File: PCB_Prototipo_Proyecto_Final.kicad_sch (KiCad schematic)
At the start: 1 part

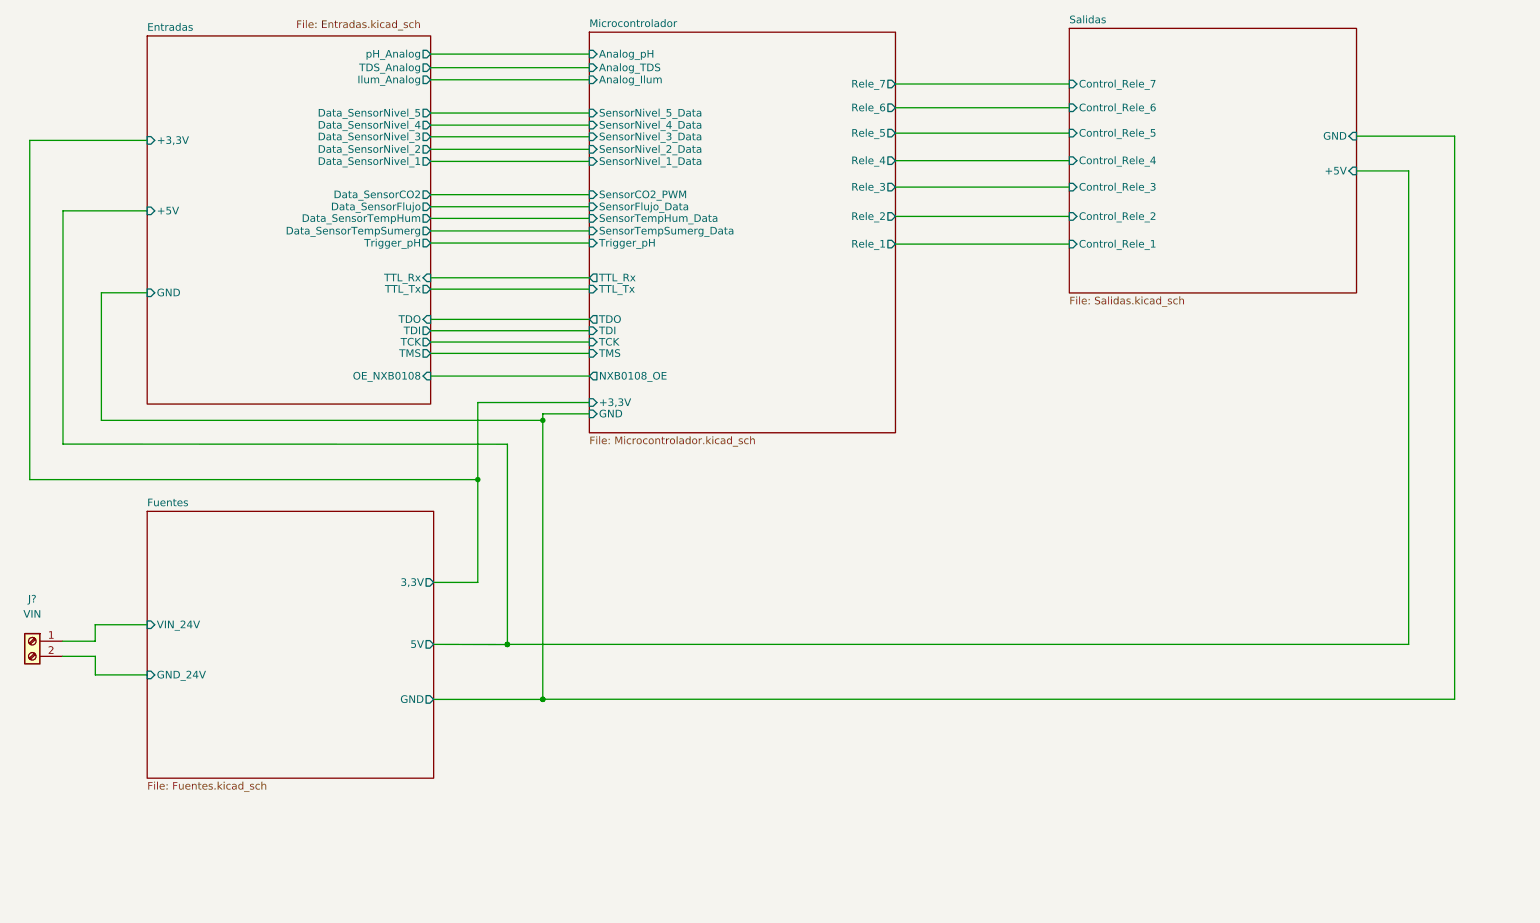
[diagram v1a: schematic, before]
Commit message: Modificación de posición de circ. filtrado y circ. de adaptación de tensión
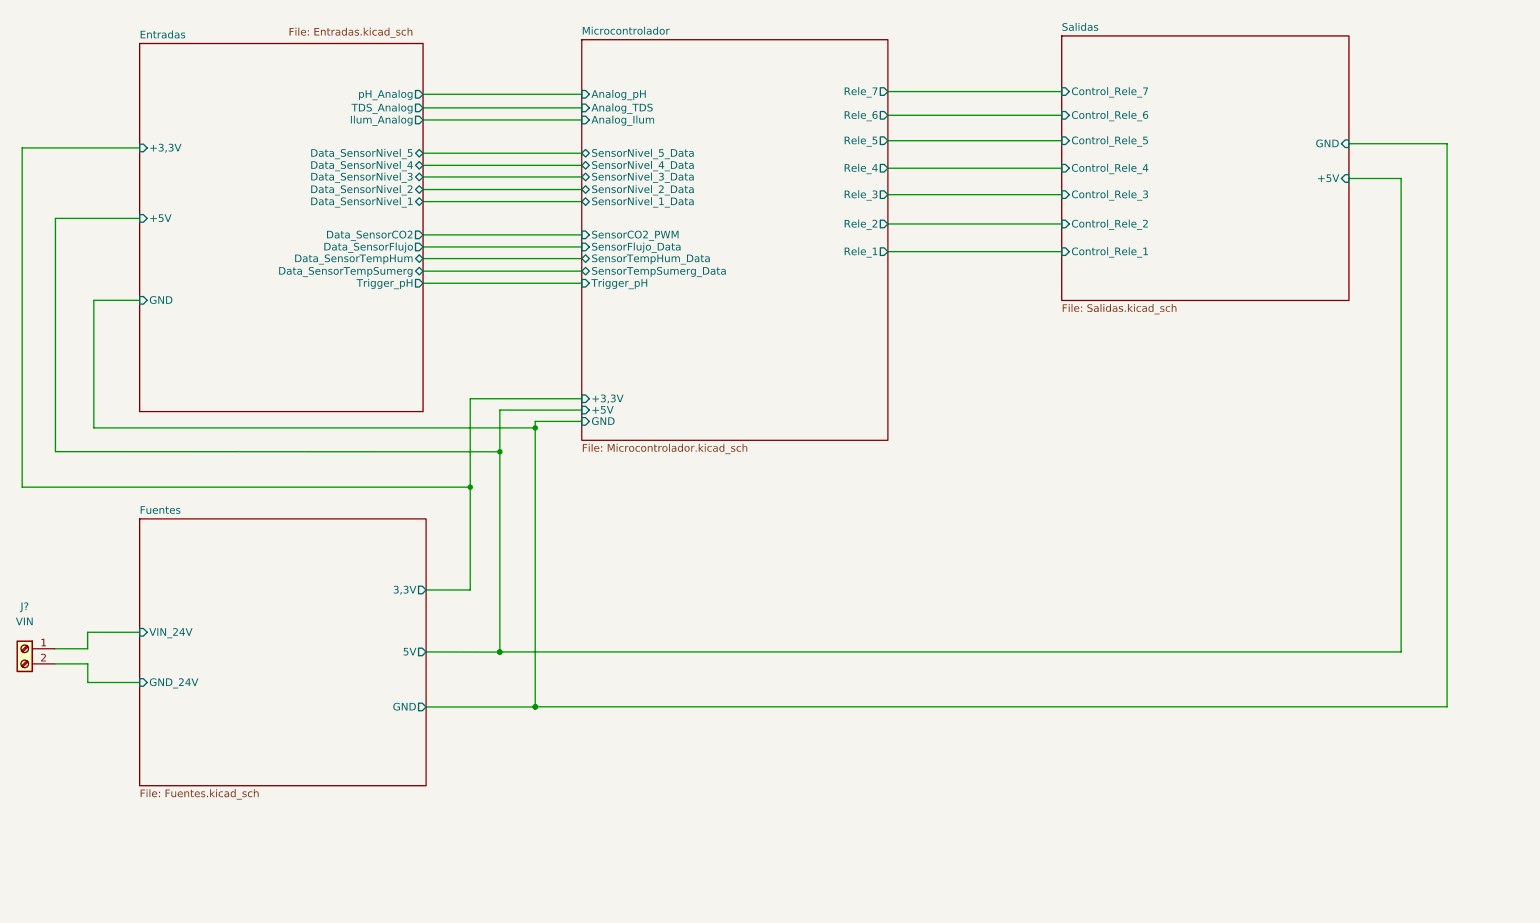
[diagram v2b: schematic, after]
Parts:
- removed J?: VIN, symbol Connector:Screw_Terminal_01x02
- added J?: VIN, symbol Connector:Screw_Terminal_01x02
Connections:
- net Fuentes/GND_24V: now also J?.2 (Pin_2)
- net Fuentes/VIN_24V: now also J?.1 (Pin_1)
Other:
- sheet Entradas ports: added none; removed OE_NXB0108, TCK, TDI, TDO, TMS, TTL_Rx, TTL_Tx
- sheet Microcontrolador ports: added +5V; removed NXB0108_OE, TCK, TDI, TDO, TMS, TTL_Rx, TTL_Tx

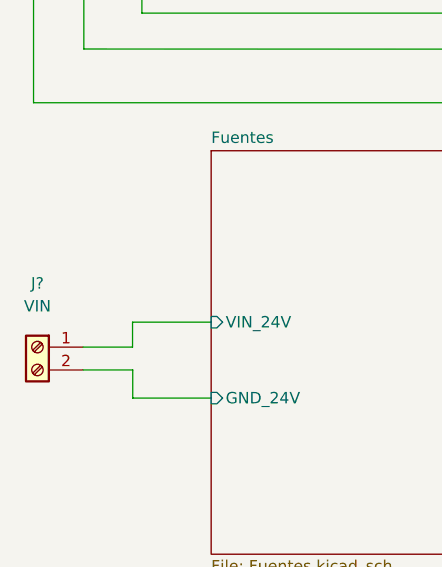
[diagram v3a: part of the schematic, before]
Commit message: Actualización de SCH según placa industrial, y búsqueda de footprints.
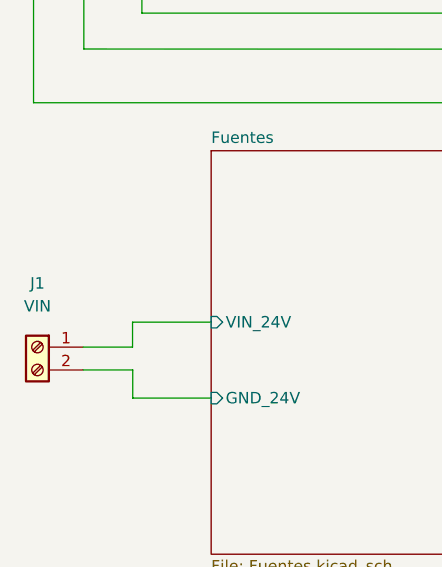
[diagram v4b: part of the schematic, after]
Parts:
- gave numbers to parts that had none: 1

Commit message: Fin de SCH, config de inicio para PCB
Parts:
- J1: footprint (none) -> TB002-500-02BE:TB00250002BE
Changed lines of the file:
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@@
     (property "Reference" "J1" (id 0) (at 29.0068 128.4986 0))
     (property "Value" "VIN" (id 1) (at 29.0068 131.0386 0))
-    (property "Footprint" "" (id 2) (at 29.0068 135.5852 0)
+    (property "Footprint" "TB002-500-02BE:TB00250002BE" (id 2) (at 29.0068 135.5852 0)
       (effects (font (size 1.27 1.27)) hide)
     )
@@
     )
     (path "/aa68080b-efaa-40f4-b3b3-094ea26c340f/c0cfa6fa-a0c7-497c-ac2e-21e840ad96c4"
-      (reference "IC1") (unit 1) (value "MCP6486T-E_OT") (footprint "")
+      (reference "IC1") (unit 1) (value "MCP6486T-E_OT") (footprint "MCP6486T-E_OT:MCP6486RT-E&slash_OT")
     )
     (path "/a0576404-cb4a-49f6-90f5-cb8b3d39ab54"
-      (reference "J1") (unit 1) (value "VIN") (footprint "")
+      (reference "J1") (unit 1) (value "VIN") (footprint "TB002-500-02BE:TB00250002BE")
     )
     (path "/922c0b39-92cb-4463-9d8d-3032074eda8e/ceaa7ae2-f24e-4663-81f0-45d9e5b0e51e"
-      (reference "J2") (unit 1) (value "Conn_01x15") (footprint "Connector_JST:JST_SUR_SM08B-SURS-TF_1x08-1MP_P0.80mm_Horizontal")
+      (reference "J2") (unit 1) (value "Conn_01x15") (footprint "Connector_PinHeader_2.54mm:PinHeader_1x15_P2.54mm_Vertical")
     )
     (path "/922c0b39-92cb-4463-9d8d-3032074eda8e/a5472214-5301-44d4-a09a-15965a4cb03f"
-      (reference "J3") (unit 1) (value "Conn_01x15") (footprint "Connector_JST:JST_SUR_SM08B-SURS-TF_1x08-1MP_P0.80mm_Horizontal")
+      (reference "J3") (unit 1) (value "Conn_01x15") (footprint "Connector_PinHeader_2.54mm:PinHeader_1x15_P2.54mm_Vertical")
     )
     (path "/aa68080b-efaa-40f4-b3b3-094ea26c340f/5d9a8247-729d-4386-8b3a-ec2849dcae66"

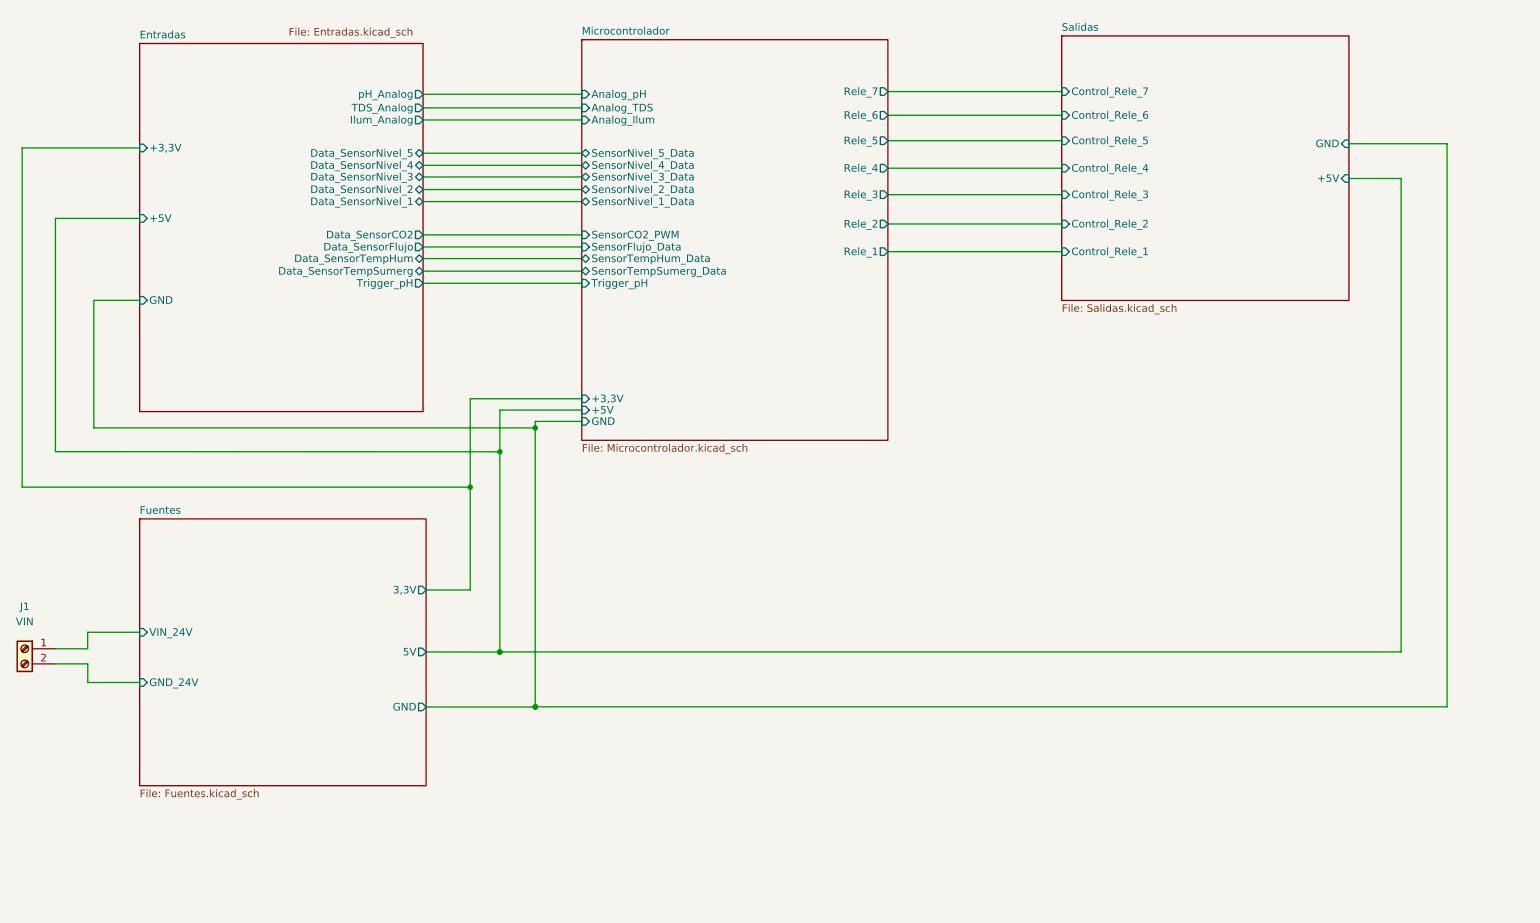
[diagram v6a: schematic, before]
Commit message: Se finalizó con el PCB del prototipo.
Dado que se buscó a toda costa que el PCB fuera de 1 capa, en varios puntos del circuito se tuvieron que agregar pin headers individuales para conectar a 3V3 y GND, junto con tiras de pin headers. Cada una de estas se conectara luego entre si mediante cables.

Tambien se generaron los archivos Gerber y BOM.
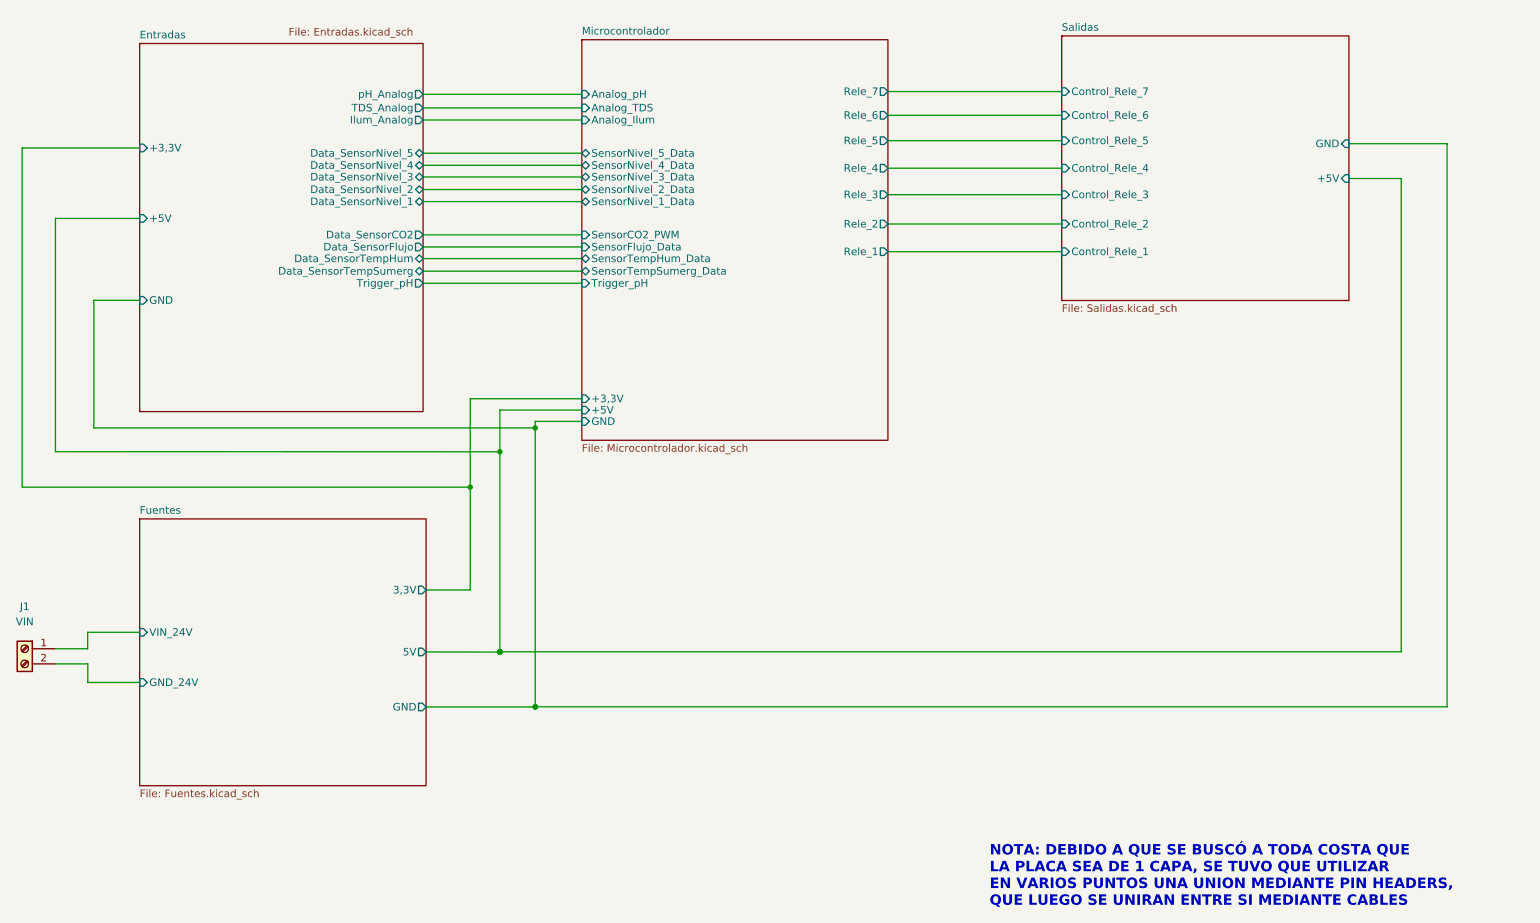
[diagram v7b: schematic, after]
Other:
- note added: "NOTA: DEBIDO A QUE SE BUSCÓ A TODA COSTA QUE LA PLACA SEA DE 1 CAPA, SE TUVO QUE UTILIZAR EN VARIOS PUNTOS UNA UNION MEDIANTE PIN HEADERS, QUE LUEGO SE UNIRAN ENTRE SI MEDIANTE CABLES"

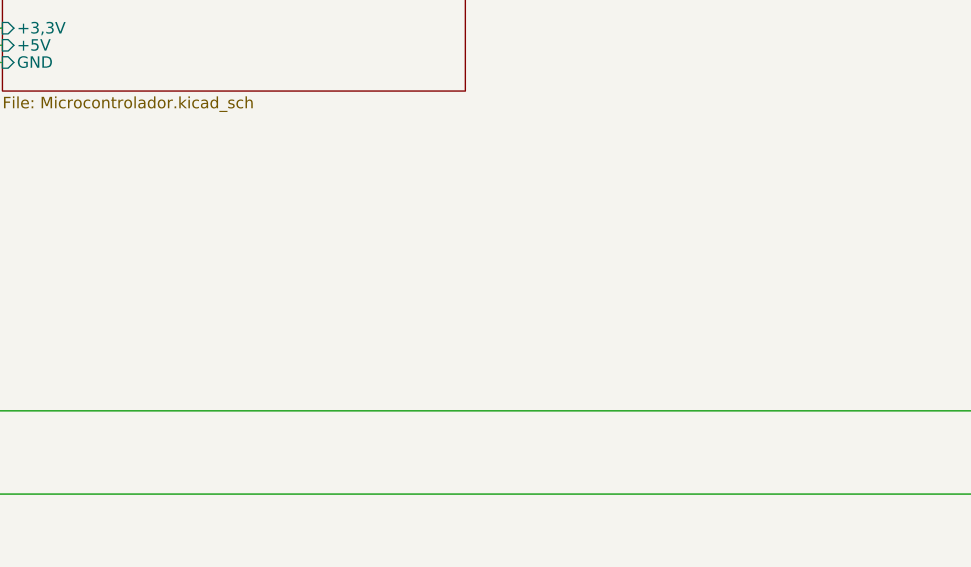
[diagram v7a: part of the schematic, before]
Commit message: Se modificaron los footprints del capacitor de 470 uF y del LM1117.
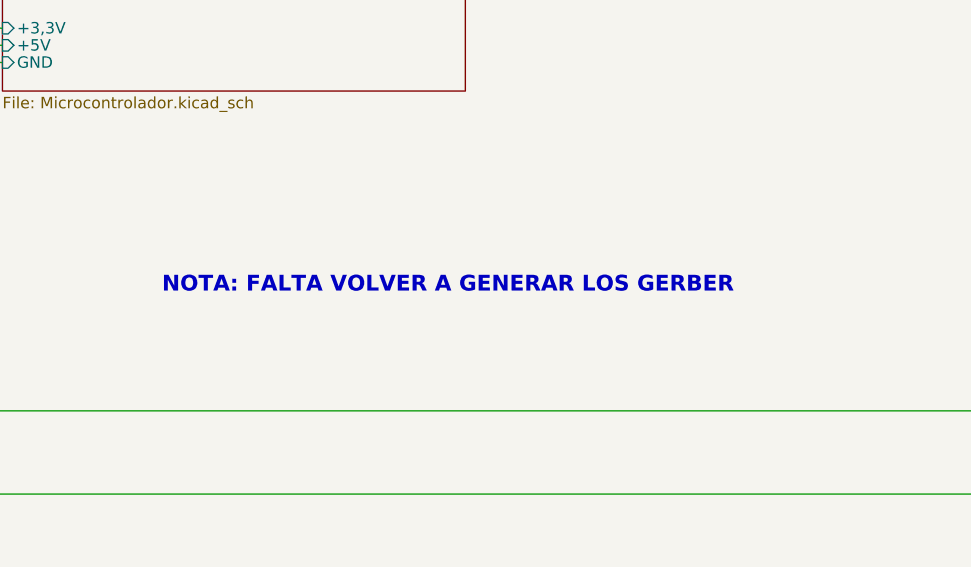
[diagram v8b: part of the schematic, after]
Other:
- note added: "NOTA: FALTA VOLVER A GENERAR LOS GERBER"
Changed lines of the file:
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@@
+    (effects (font (size 1.75 1.75) (thickness 0.254) bold) (justify left bottom))
+  )
+  (text "NOTA: FALTA VOLVER A GENERAR LOS GERBER" (at 140.335 123.19 0)
     (effects (font (size 1.75 1.75) (thickness 0.254) bold) (justify left bottom))
   )
@@
     )
     (path "/5f92bd8c-6854-4ae3-a1d0-b070a0d6afe8/12fc8e7b-24ff-4986-8408-7534acd8b9e1"
-      (reference "C14") (unit 1) (value "470 uF, 50V") (footprint "UUG1H471MNQ6MS:CAPAE1710X1750N")
+      (reference "C14") (unit 1) (value "470 uF, 50V") (footprint "VE-471M1HTR-1316:CAPAE1300X1650N")
     )
     (path "/5f92bd8c-6854-4ae3-a1d0-b070a0d6afe8/af5e945d-6e41-491f-943f-f54ce556d497"
@@
     )
     (path "/5f92bd8c-6854-4ae3-a1d0-b070a0d6afe8/1d996468-537d-448d-b463-fef17f9a74b3"
-      (reference "U2") (unit 1) (value "LM1117-3.3") (footprint "LM1117MPX-33NOPB:SOT230P700X180-4N")
+      (reference "U2") (unit 1) (value "LM1117-3.3") (footprint "LM1117SX-3V3-NOPB:KTT0003B")
     )
     (path "/922c0b39-92cb-4463-9d8d-3032074eda8e/b47a20aa-eb34-4145-a72d-b3dac59fdda6/a97a44f5-b6f4-4f21-8daf-f76df10ef6c3"
